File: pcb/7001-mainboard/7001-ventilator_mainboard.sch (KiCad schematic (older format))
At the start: 92 parts, among them J1 USB_B_Micro, J10 UART, J11 I2C, J12 FLOW_SENSORS, J13 PREG_PWR, J14 PREG_PWR, J2 SWD, J3 12V, J4 DNI, J5 24VIN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

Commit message: Cleanup BOM, sync with schematic, prepare layout
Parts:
- added TP4: DNI, TestPoint:TestPoint_THTPad_D1.5mm_Drill0.7mm, symbol Connector:TestPoint
- C18, C21, C38, C42, C44: footprint Capacitor_SMD:C_1206_3216Metric -> Capacitor_SMD:C_1210_3225Metric
- C7: Note rc time must be faster than boot_ISP -> (none); purpose reset debounce/protection -> reset debounce/protection + time delay on POR
- J1: Farnell (none) -> 1568026; MPN (none) -> 47346-0001
- J10: value UART -> 4-pin header
- J11: value I2C -> 4-pin screw terminal; Farnell (none) -> 1841317; MPN (none) -> 691322110004
- J12: value FLOW_SENSORS -> 3-pin screw terminal; MPN (none) -> 691322110003; Mouser (none) -> 710-691322110003
- J13, J14, J7: value PREG_PWR -> 2-pin screw terminal; Farnell (none) -> 1841315; MPN (none) -> 691322110002
- J2: value SWD -> 4-pin header
- J3: value 12V -> 2-pin screw terminal; Farnell (none) -> 1841315; MPN (none) -> 691322110002
- J5: value 24VIN -> 2-pin screw terminal; Farnell (none) -> 1841315; MPN (none) -> 691322110002
- J8: value PREG_SIGNALS -> 3-pin screw terminal; MPN (none) -> 691322110003; Mouser (none) -> 710-691322110003
- J9: footprint Connector_PinSocket_2.54mm:PinSocket_2x20_P2.54mm_Vertical_SMD -> Connector_PinSocket_2.54mm:PinSocket_2x20_P2.54mm_Vertical
- TP1, TP5: value 5V -> DNI
- U2: Farnell (none) -> 3116500; MPN (none) -> TPD2E2U06DRLR
- U3: Farnell (none) -> 2115662; MPN (none) -> LPC11U37FBD48/401
- U5: footprint (none) -> Jitter_Footprints:DCDC-5V_S24SE05004PDFA
- U6: Current Rating (none) -> Limited by power dissipation. 40mA would dissipate 0.5W, do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
- Y1: value MCSJK-7U-12.00-10-10-80-B-10 -> 12MHz; Farnell (none) -> 2308719; MPN (none) -> 7M-12.000MEEQ-T
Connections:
- net labels removed: pwm_1, pwm_2
- wire segments 254 -> 259
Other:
- note added: "2x 24V output"
- note added: "4-20mA DAC to control\nthe pressure regulator.\nThe regulator also gives\na feedback signal 4-20mA.\n\nThe feedback is not used\ndirectly for control, but\ncan be used as sanity check."
- note added: "5v servo header?"
- note added: "CT16B0_MAT0"
- note added: "NOTE: LPC11u is 3.3V,\nbut 5v-tolerant for I2C;\noptional I2C-based flow sensors \nallow 2.5V as digital high;\npressure sensor is 3.3V-based,\nunknown if 5V-tolerant"
- note added: "TODO\n\n- test points\n- Any remaining GPIO/ADC on header"
- note removed: "4-20mA DAC to controll\nthe pressure regulator.\nThe regulator also gives\na feedback signal 4-20mA.\n\nThe feedback is not used\ndirectly for control, but\ncan be used as sanity check."
- note removed: "NOTE: LPC11u is 3.3V but 5v-tolerant for I2C,\noptional I2C-based flow sensors allow 2.5V as digital high\npressure sensor is 3.3V-based, unknown if 5V-tolerant"
- note removed: "TODO\n\n- test points\n- ADC in header\n- GPIO header"
- moved on the sheet: C17, C40, C41, C42, C43, C44, C45, D1, D2, J12, J13, J14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

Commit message: update schematics from feedback
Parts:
- added C46, C47: 10nF 100V, Capacitor_SMD:C_1206_3216Metric, symbol Device:C
- added C48: 10nF, Capacitor_SMD:C_0805_2012Metric, symbol Device:C
- added C49, C50: 100nF, Capacitor_SMD:C_0805_2012Metric, symbol Device:C
- added D10: Red, LED_SMD:LED_0805_2012Metric, symbol Device:LED
- added D3: S5MB R5G 100V, symbol Device:D
- added D4, D5: D_TVS, symbol Device:D_TVS
- added D6, D7, D8, D9: Green, LED_SMD:LED_0805_2012Metric, symbol Device:LED
- added FL1: 744282010, symbol Jitter_Components:CommonModeChoke_744282010
- added J15: 6-pin header, Connector_PinHeader_2.54mm:PinHeader_2x10_P2.54mm_Vertical_SMD, symbol Connector_Generic:Conn_02x10_Odd_Even
- added R37: DNI, Resistor_SMD:R_0805_2012Metric, symbol Device:R
- added R38, R40: 3.3k, Resistor_SMD:R_0805_2012Metric, symbol Device:R
- added R39: 10k, Resistor_SMD:R_0805_2012Metric, symbol Device:R
- added R41, R42, R43: 150, Resistor_SMD:R_0805_2012Metric, symbol Device:R
- added RV1: Varistor, symbol Device:Varistor
- J10: value 4-pin header -> 6-pin header; footprint Connector_PinSocket_2.54mm:PinSocket_1x04_P2.54mm_Vertical -> Connector_PinHeader_2.54mm:PinHeader_1x06_P2.54mm_Vertical; symbol Connector_Generic:Conn_01x04 -> Connector_Generic:Conn_01x06
- R29: value 1k5 -> 3.3k
- R33: value 1k5 -> 0
- R35: value 1k5 -> 4.7k
- R6: value 68k -> 10k
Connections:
- net labels added: LED_ERROR, LED_STATUS, MCU_IO_1, MCU_IO_2, MCU_IO_3, MCU_IO_4, RPI_IO_1, RPI_IO_2, RPI_IO_3, RPI_IO_4
- wire segments 259 -> 341
- no-connect marks 36 -> 37
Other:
- note added: "->"
- note added: "<-"
- note added: "Extra I/O"
- note added: "Extra header in\ncase of changing\nrequirements"
- note added: "Jumper Option:\n1-2: power 5V from 24V DC/DC\n2-3: power 5V from USB\nNC: power 5V from Raspberry Pi\n\nin production, this jumper\ncan be left out"
- note added: "Note: do we need this?\nR6/R29 as DNI\nshould also enable\npower.."
- note added: "Power / status LEDS"
- note added: "Should be compatible\nwith TTL-232R-3V3\n\nNote: are TX/RX correct?"
- note added: "Strong pulldown: overrule\nmcu internal pullups\nto avoid glitch at power-on"
- note added: "TODO:\n\n- test points?\n- fiducials"
- note removed: "Jumper Option:\n1-2: power 5V from 24V DC/DC\n2-3: power 5V from USB\nNC: power 5V from Raspberry Pi"
- note removed: "TODO DIFFERENT UART?"
- note removed: "TODO\n\n- test points\n- Any remaining GPIO/ADC on header"
- note removed: "floating input\nshould also\nenable power"
- moved on the sheet: C1, C10, C11, C12, C13, C16, C17, C18, C19, C2, C22, C25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

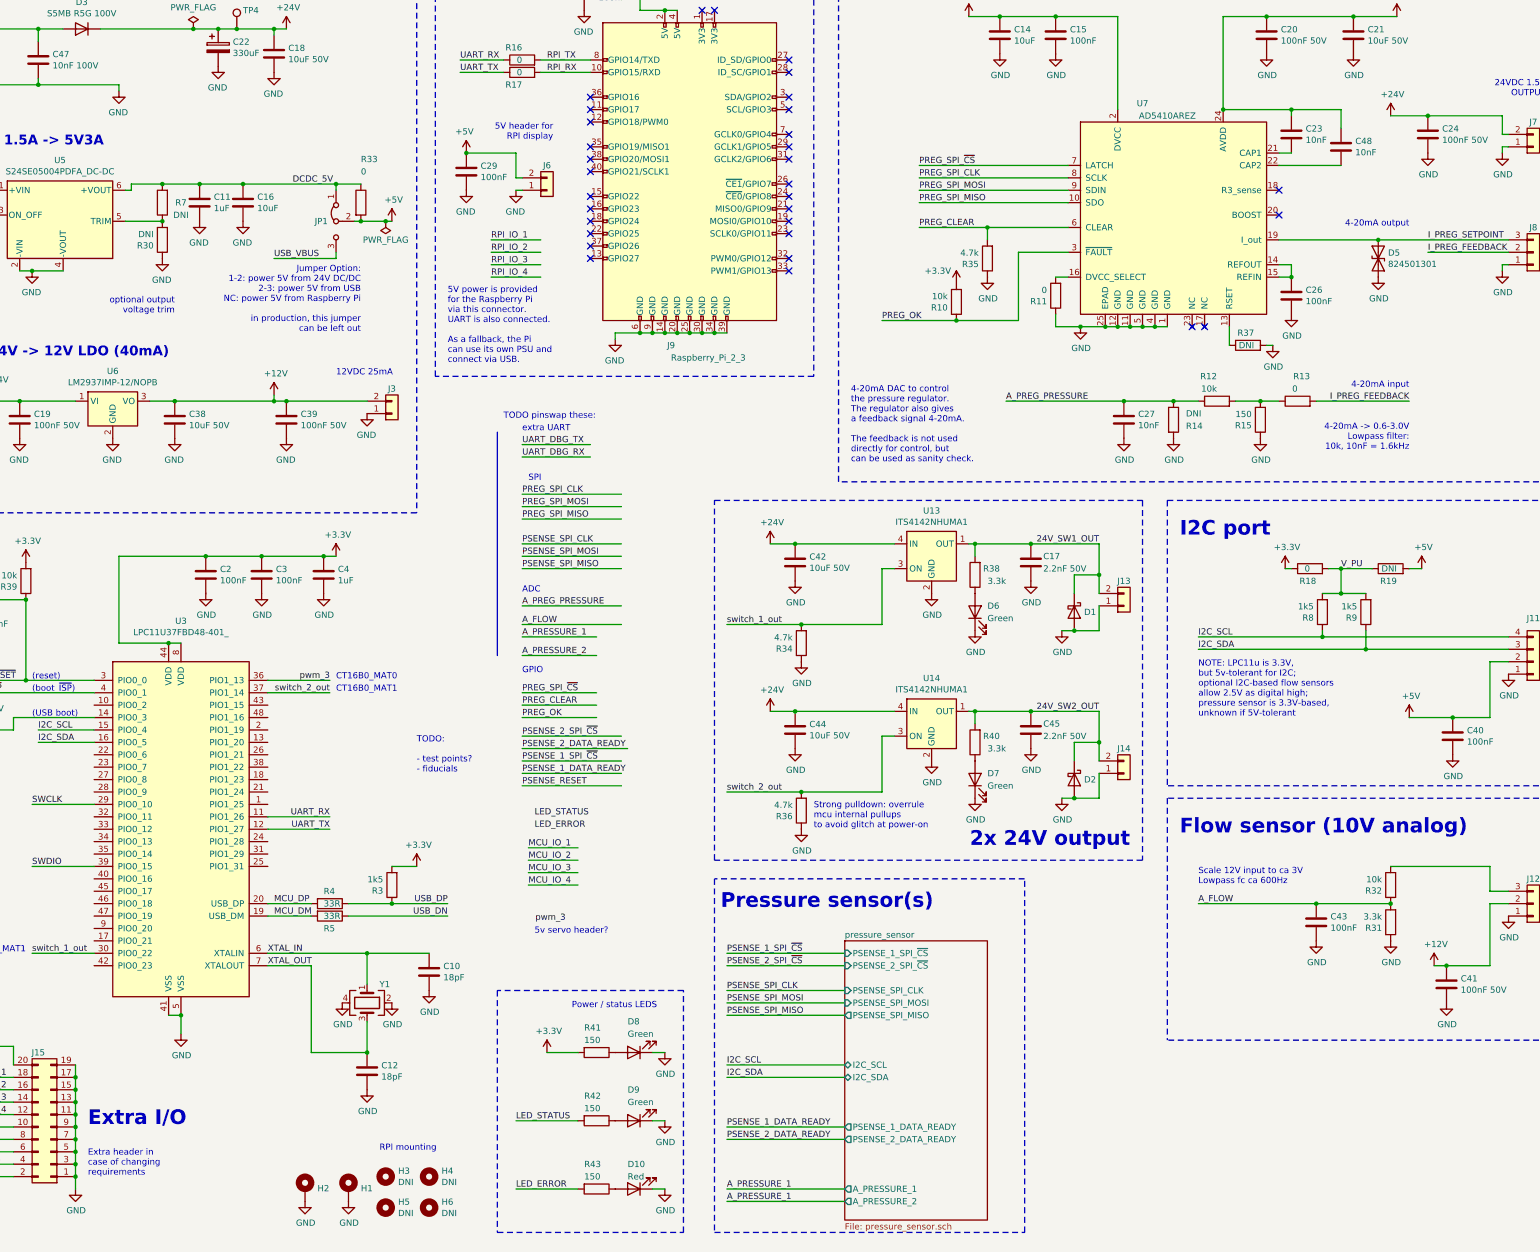
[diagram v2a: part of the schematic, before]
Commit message: Update schematics based on more feedback
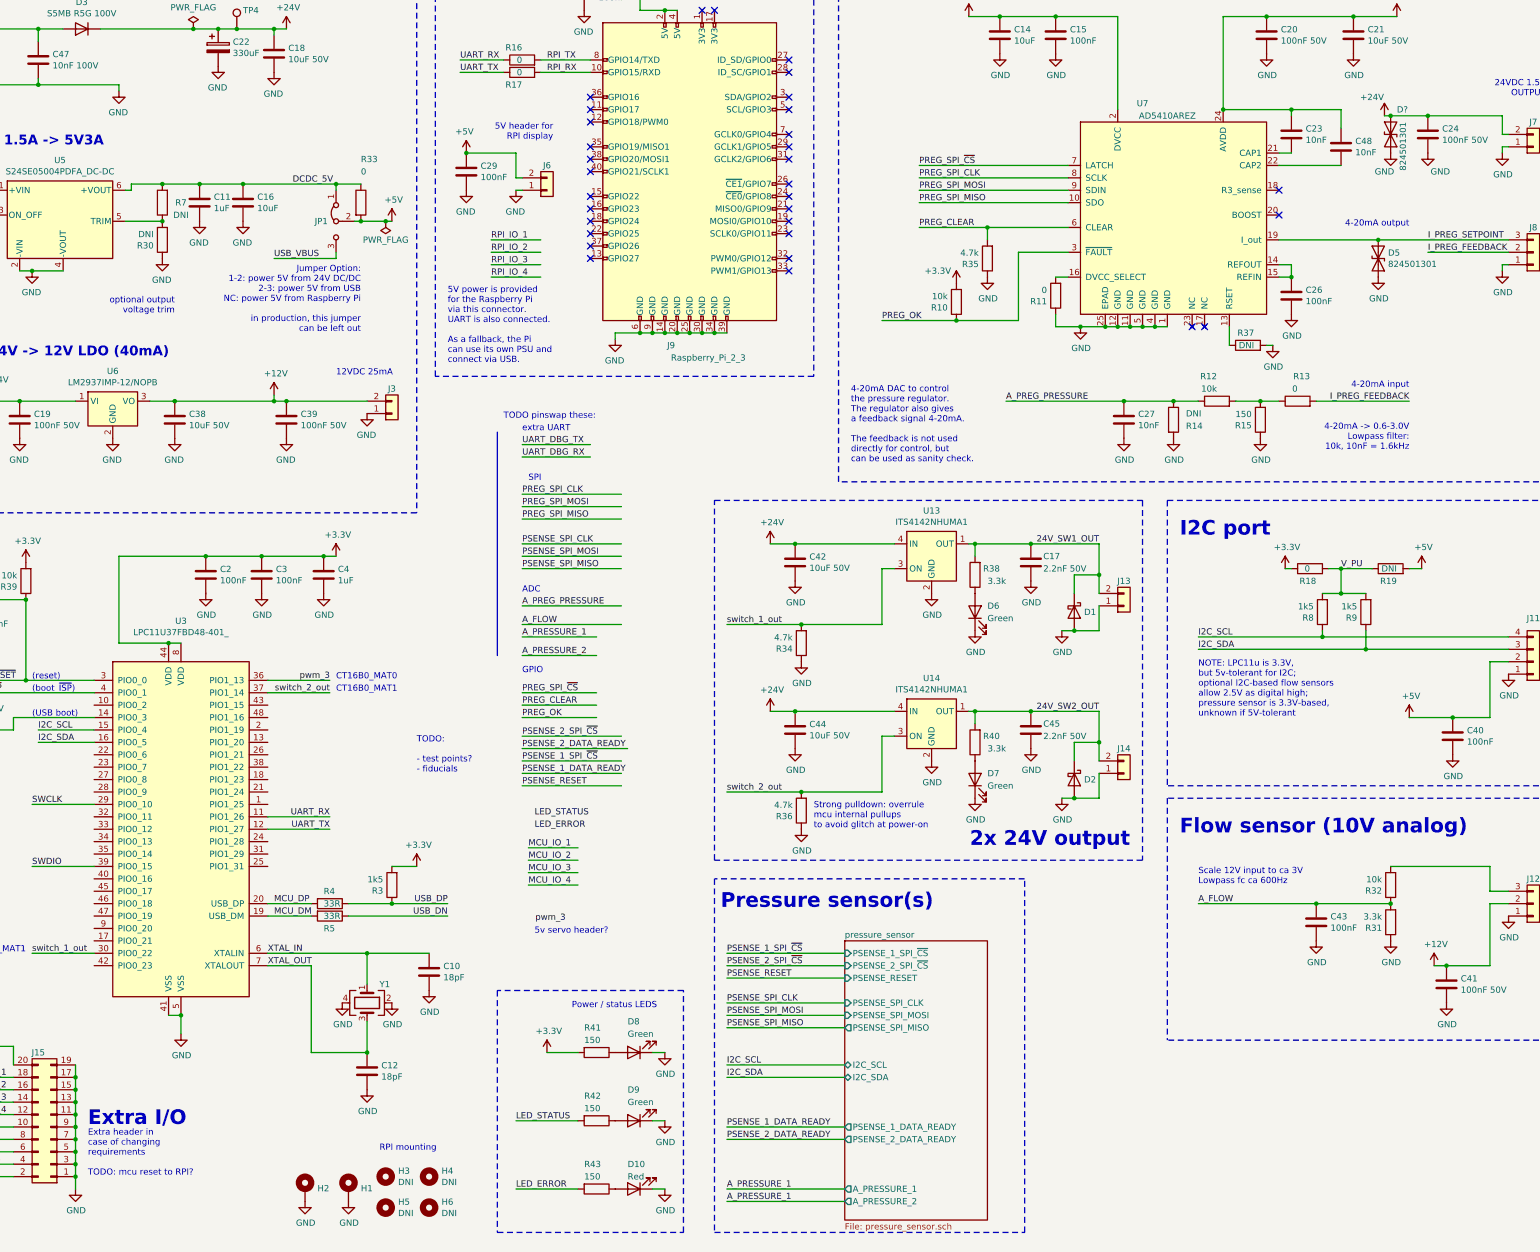
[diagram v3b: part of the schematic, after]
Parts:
- added D?: D_TVS, symbol Device:D_TVS
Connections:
- wire segments 341 -> 343
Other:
- note added: "Extra header in\ncase of changing\nrequirements\n\nTODO: mcu reset to RPI?"
- note removed: "Extra header in\ncase of changing\nrequirements"
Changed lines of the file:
@@
 AR Path="/5EB202B5" Ref="#PWR013"  Part="1"
 F 0 "#PWR013" H 14850 2150 50  0001 C CNN
-F 1 "GND" H 14855 2227 50  0000 C CNN
+F 1 "GND" H 14950 2250 50  0000 C CNN
 F 2 "" H 14850 2400 50  0001 C CNN
 F 3 "" H 14850 2400 50  0001 C CNN
@@
 L power:+24V #PWR012
 U 1 1 5EC9A4D0
-P 14550 2100
-F 0 "#PWR012" H 14550 1950 50  0001 C CNN
-F 1 "+24V" H 14565 2273 50  0000 C CNN
-F 2 "" H 14550 2100 50  0001 C CNN
-F 3 "" H 14550 2100 50  0001 C CNN
-	1    14550 2100
+P 14500 2100
+F 0 "#PWR012" H 14500 1950 50  0001 C CNN
+F 1 "+24V" H 14400 2250 50  0000 C CNN
+F 2 "" H 14500 2100 50  0001 C CNN
+F 3 "" H 14500 2100 50  0001 C CNN
+	1    14500 2100
 	1    0    0    -1
 $EndComp
@@
 F2 "PSENSE_2_DATA_READY" O L 10150 10350 50
 F3 "PSENSE_2_SPI_~CS~" I L 10150 8950 50
-F4 "PSENSE_SPI_CLK" I L 10150 9150 50
-F5 "PSENSE_SPI_MOSI" I L 10150 9250 50
-F6 "PSENSE_SPI_MISO" O L 10150 9350 50
+F4 "PSENSE_SPI_CLK" I L 10150 9250 50
+F5 "PSENSE_SPI_MOSI" I L 10150 9350 50
+F6 "PSENSE_SPI_MISO" O L 10150 9450 50
 F7 "PSENSE_1_DATA_READY" O L 10150 10250 50
 F8 "I2C_SCL" B L 10150 9750 50
@@
 F11 "A_PRESSURE_1" O L 10150 10750 50
 F12 "PSENSE_1_SPI_~CS~" I L 10150 8850 50
+F13 "PSENSE_RESET" I L 10150 9050 50
 $EndSheet
 Text Label 9200 10350 0    50   ~ 0
@@
 Text Label 9200 8850 0    50   ~ 0
 PSENSE_1_SPI_~CS~
-Text Label 9200 9150 0    50   ~ 0
+Text Label 9200 9250 0    50   ~ 0
 PSENSE_SPI_CLK
-Text Label 9200 9250 0    50   ~ 0
+Text Label 9200 9350 0    50   ~ 0
 PSENSE_SPI_MOSI
-Text Label 9200 9350 0    50   ~ 0
+Text Label 9200 9450 0    50   ~ 0
 PSENSE_SPI_MISO
 Wire Wire Line
-	9200 9350 10150 9350
-Wire Wire Line
-	10150 9250 9200 9250
-Wire Wire Line
-	9200 9150 10150 9150
+	9200 9450 10150 9450
+Wire Wire Line
+	10150 9350 9200 9350
+Wire Wire Line
+	9200 9250 10150 9250
 Wire Wire Line
 	9200 8950 10150 8950
@@
 RPI_IO_4
 Text Notes 4050 10650 0    50   ~ 0
-Extra header in\ncase of changing\nrequirements
+Extra header in\ncase of changing\nrequirements\n\nTODO: mcu reset to RPI?
 Text Notes 6700 7400 0    50   ~ 0
 TODO:\n\n- test points?\n- fiducials
@@
 	1    0    0    -1
 $EndComp
+$Comp
+L Device:D_TVS D?
+U 1 1 5F60AF83
+P 14550 2250
+F 0 "D?" V 14750 2200 50  0000 R CNN
+F 1 "D_TVS" V 14505 2171 50  0001 R CNN
+F 2 "" H 14550 2250 50  0001 C CNN
+F 3 "~" H 14550 2250 50  0001 C CNN
+F 4 "824501301" H 14650 2150 50  0000 R CNN "MPN"
+	1    14550 2250
+	0    -1   -1   0
+$EndComp
+$Comp
+L power:GND #PWR?
+U 1 1 5F60AF89
+P 14550 2400
+AR Path="/5BF2E340/5F60AF89" Ref="#PWR?"  Part="1"
+AR Path="/5F60AF89" Ref="#PWR?"  Part="1"
+F 0 "#PWR?" H 14550 2150 50  0001 C CNN
+F 1 "GND" H 14500 2250 50  0000 C CNN
+F 2 "" H 14550 2400 50  0001 C CNN
+F 3 "" H 14550 2400 50  0001 C CNN
+	1    14550 2400
+	1    0    0    -1
+$EndComp
+Wire Wire Line
+	14500 2100 14550 2100
+Connection ~ 14550 2100
+Wire Wire Line
+	10150 9050 9200 9050
+Text Label 9200 9050 0    50   ~ 0
+PSENSE_RESET
 $EndSCHEMATC

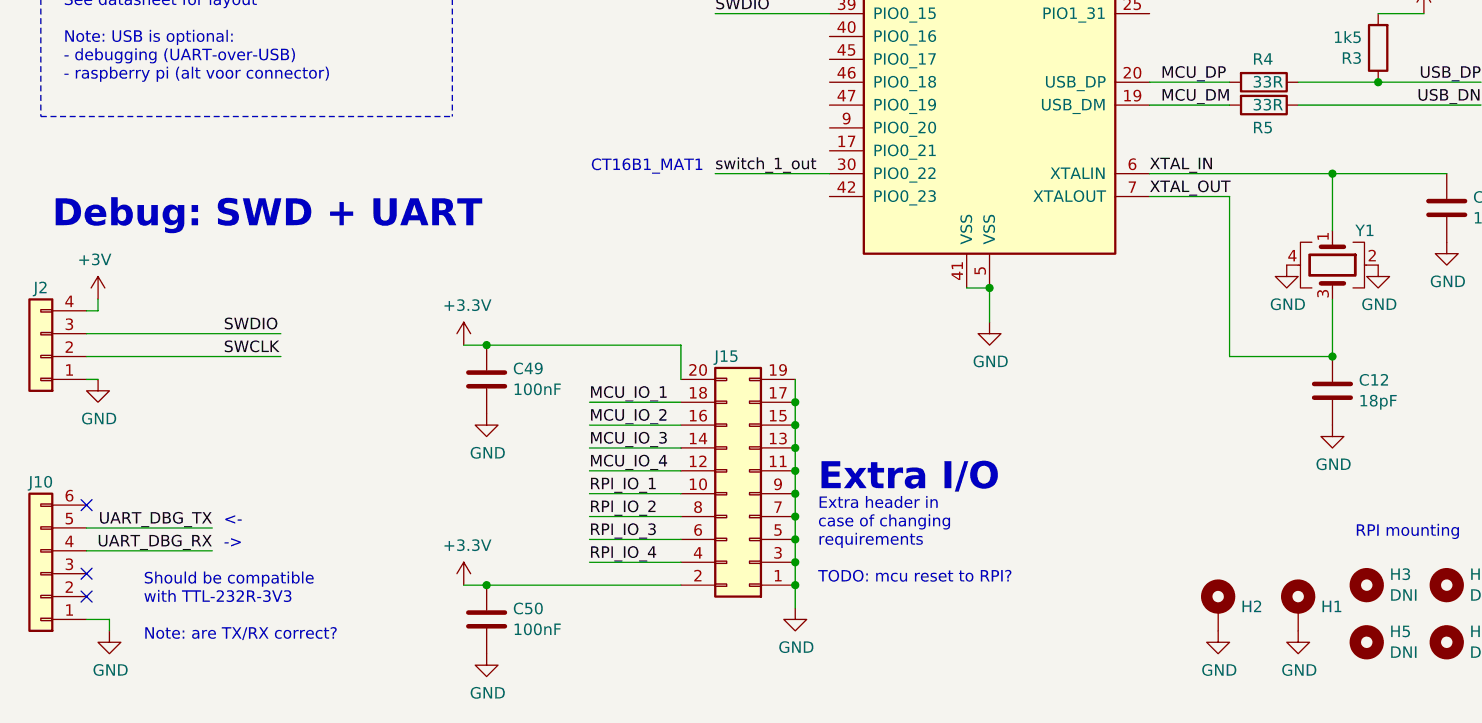
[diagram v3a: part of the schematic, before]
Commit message: Add 10-pin SWD connector, SMD connector for RPI
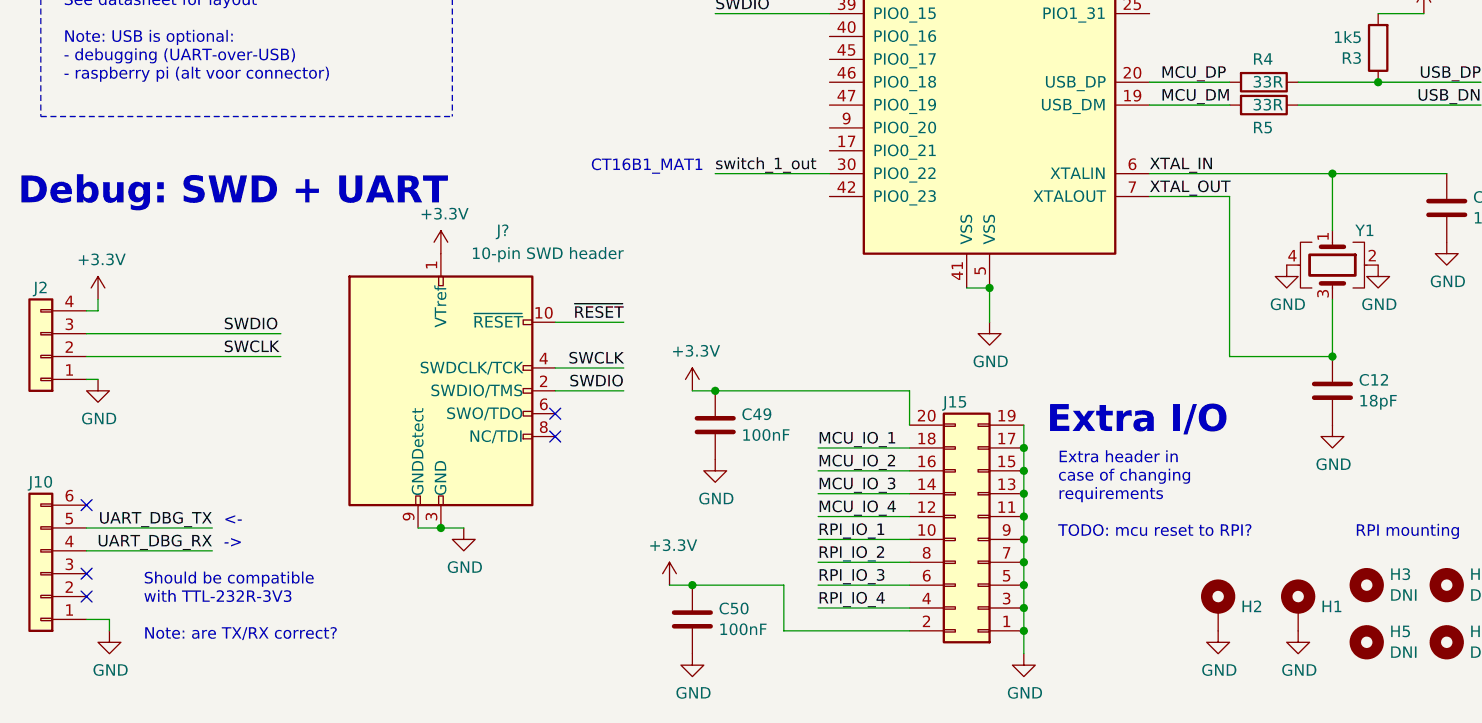
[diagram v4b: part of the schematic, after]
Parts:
- added J?: 10-pin SWD header, Jitter_Footprints:connector_jtag_10pin_shrouded, symbol Connector:Conn_ARM_JTAG_SWD_10
- J9: footprint Connector_PinSocket_2.54mm:PinSocket_2x20_P2.54mm_Vertical -> (none); Farnell (none) -> 2827937; MPN (none) -> 610020243021
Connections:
- net labels removed: +3V
- wire segments 343 -> 350
- no-connect marks 37 -> 39
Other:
- moved on the sheet: C49, C50, J15
